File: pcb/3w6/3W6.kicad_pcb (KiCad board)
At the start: 2 copper layers, 243.2 x 106 mm, 113 parts, among them J1 USB_C Main, J2 USB_C I2C_L, J3 USB_C I2C_R, SW1 SW_Push, SW10 SW_Push, SW11 SW_Push, SW12 SW_Push, SW13 SW_Push, SW14 SW_Push, SW15 SW_Push, SW16 SW_Push, SW17 Trackball_Choc_Combi, SW18 SW_Push, SW19 SW_Push, SW2 SW_Push, SW20 SW_Push, SW21 SW_Push, SW22 SW_Push, SW23 SW_Push, SW24 SW_Push, SW25 SW_Push, SW26 SW_Push, SW27 SW_Push, SW28 SW_Push, SW29 SW_Push, SW3 SW_Push, SW30 SW_Push, SW31 SW_Push, SW32 SW_Push, SW33 SW_Push, SW34 SW_Push, SW35 SW_Push, SW36 SW_Push, SW37 SW_Push, SW4 SW_Push, SW5 SW_Push, SW6 SW_Push, SW7 SW_Push, SW8 SW_Push, SW9 SW_Push, U1 ATmega32U4-AU, U2 TCA9535PWR, Y1 16MHZ

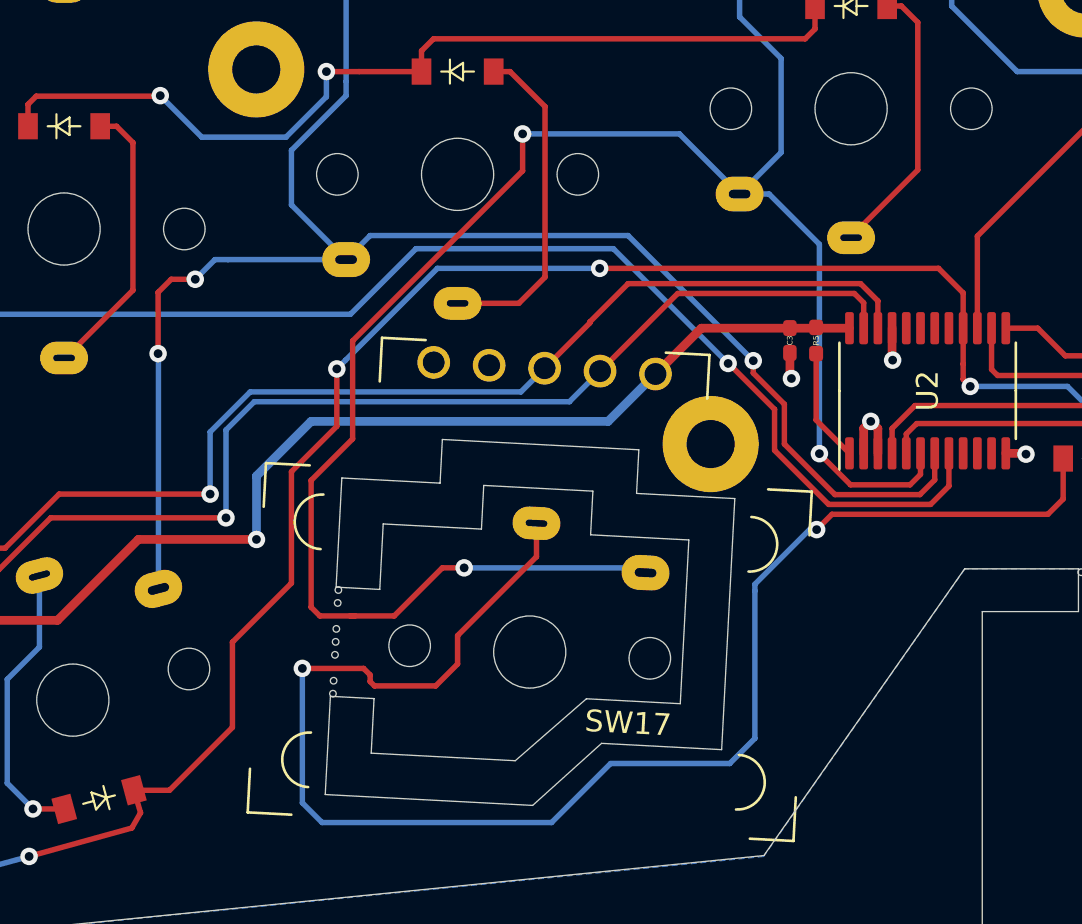
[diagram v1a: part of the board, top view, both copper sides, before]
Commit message: fix problems from last production run
changed IO-Expander to PCA9555
moved some vias to connect the copper island around the pimoroni GND pin to board GND
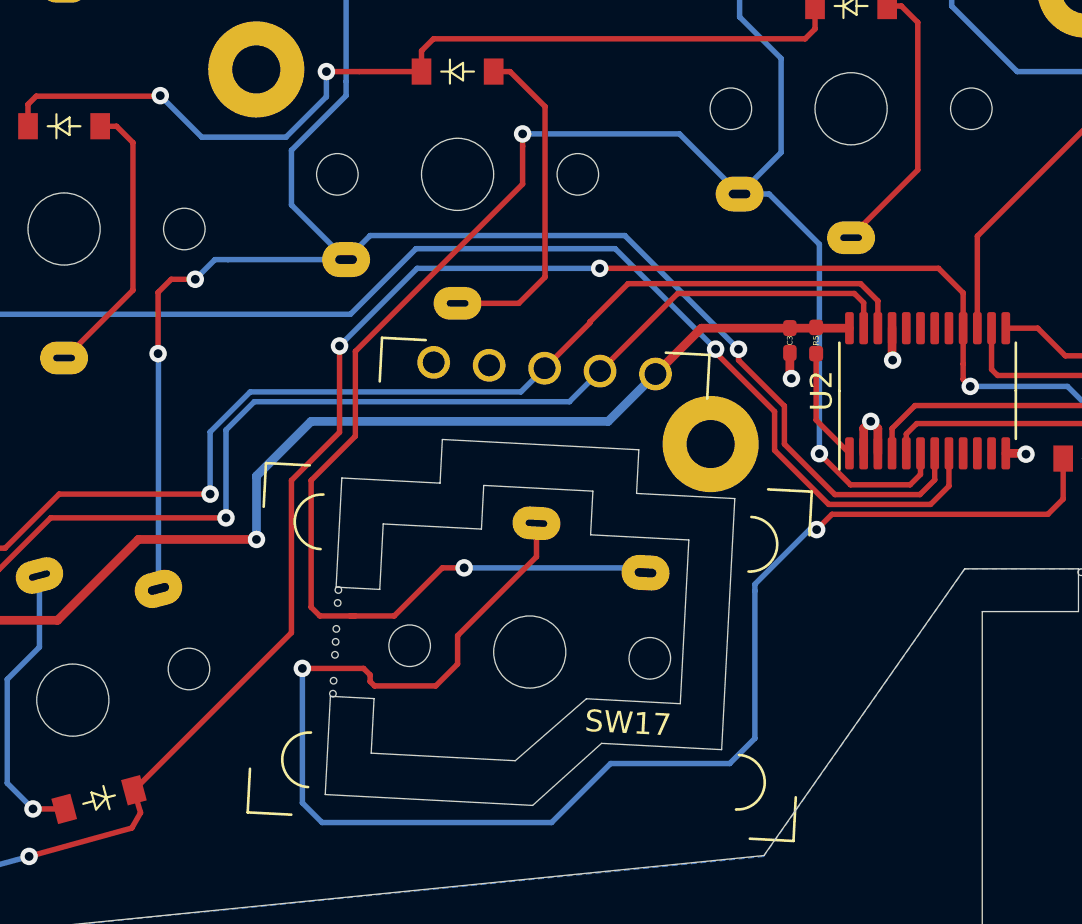
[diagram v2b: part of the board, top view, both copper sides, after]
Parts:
- U2: value TCA9535PWR -> PCA9555PW
